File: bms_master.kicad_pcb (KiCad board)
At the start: 4 copper layers, 0 parts

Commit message: SCH[Sens & Inputs, Logic]: Started on sens and inputs condtiong, Logic page drawn. Need to add notes still.
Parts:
- added C1: 0.1 µF, remote_cl05a105ko5nnnc:C_0402_1005Metric, F.Cu at (155.5, 102.0)
- added C10: 0.1 µF, remote_cl05a105ko5nnnc:C_0402_1005Metric, F.Cu at (174.5, 97.9)
- added C11: 100 pF, remote_cl05a105ko5nnnc:C_0402_1005Metric, F.Cu at (150.6, 95.9)
- added C12: 100 pF, remote_cl05a105ko5nnnc:C_0402_1005Metric, F.Cu at (150.6, 97.9)
- added C13: 100 pF, remote_cl05a105ko5nnnc:C_0402_1005Metric, F.Cu at (150.6, 99.8)
- added C14: 100 pF, remote_cl05a105ko5nnnc:C_0402_1005Metric, F.Cu at (150.6, 101.8)
- added C15: 0.1 µF, remote_cl05a105ko5nnnc:C_0402_1005Metric, F.Cu at (155.5, 107.9)
- added C2: 4.7 nF, remote_cga3e3x7r1h474k080ae:C_0603_1608Metric, F.Cu at (160.3, 92.2)
- added C3: 0.1 µF, remote_cl05a105ko5nnnc:C_0402_1005Metric, F.Cu at (155.5, 104.0)
- added C4: 0.1 µF, remote_cl05a105ko5nnnc:C_0402_1005Metric, F.Cu at (155.5, 105.9)
- added C5: 100pF, remote_cl05a105ko5nnnc:C_0402_1005Metric, F.Cu at (150.6, 92.0)
- added C6: 100pF, remote_cl05a105ko5nnnc:C_0402_1005Metric, F.Cu at (150.6, 93.9)
- added C7: 220 nF, remote_cl05a105ko5nnnc:C_0402_1005Metric, F.Cu at (174.5, 92.0)
- added C8: 0.1 µF, remote_cl05a105ko5nnnc:C_0402_1005Metric, F.Cu at (174.5, 93.9)
- added C9: 220 nF, remote_cl05a105ko5nnnc:C_0402_1005Metric, F.Cu at (174.5, 95.9)
- added D1: PESD5V0U2BT-QR, remote_pesd5v0u2bt-qr:SOT-23-3, F.Cu at (148.8, 105.1)
- added D2: PESD5V0U2BT-QR, remote_pesd5v0u2bt-qr:SOT-23-3, F.Cu at (148.8, 109.6)
- added D3: Green, remote_ltst-c190tbkt:LED_0603_1608Metric, F.Cu at (156.3, 92.2)
- added D4: Green, remote_ltst-c190tbkt:LED_0603_1608Metric, F.Cu at (156.3, 94.7)
- added D5: RED, remote_ltst-c190tbkt:LED_0603_1608Metric, F.Cu at (156.3, 97.3)
- added D6: RED, remote_ltst-c190tbkt:LED_0603_1608Metric, F.Cu at (156.3, 99.8)
- added J1: 0436500200, remote_0436500200:CONN_SD-43650-001_02_MOL, F.Cu at (142.2, 79.2)
- added J2: 0430450200, remote_0430450200:CONN_SD-43045-001_02_MOL, F.Cu at (166.7, 65.1)
- added J3: TFM-115-02-S-D-WT, remote_tfm-115-02-s-d-wt:SAMTEC_TFM-115-02-S-D-WT, F.Cu at (148.6, 64.5)
- added J4: TFM-115-02-S-D-WT, remote_tfm-115-02-s-d-wt:SAMTEC_TFM-115-02-S-D-WT, F.Cu at (148.6, 72.9)
- added J7: 0436500600, remote_0436500600:CONN_SD-43650-001_06_MOL, F.Cu at (166.8, 79.2)
- added R1: 1k, remote_erj-2ge0r00x:R_0402_1005Metric, F.Cu at (147.7, 92.0)
- added R10: 1k, remote_erj-2ge0r00x:R_0402_1005Metric, F.Cu at (163.8, 92.0)
- added R11: 1k, remote_erj-2ge0r00x:R_0402_1005Metric, F.Cu at (163.8, 94.0)
- added R12: 10k, remote_erj-2ge0r00x:R_0402_1005Metric, F.Cu at (163.8, 96.0)
- added R13: 100k, remote_rcs060359r0fkea:R_0603_1608Metric, F.Cu at (160.3, 94.7)
- added R14: 10k, remote_erj-2ge0r00x:R_0402_1005Metric, F.Cu at (166.7, 92.0)
- added R15: 10k, remote_erj-2ge0r00x:R_0402_1005Metric, F.Cu at (166.7, 94.0)
- added R16: 10k, remote_erj-2ge0r00x:R_0402_1005Metric, F.Cu at (166.7, 96.0)
- added R17: 10k, remote_erj-2ge0r00x:R_0402_1005Metric, F.Cu at (169.6, 92.0)
- added R18: 1k, remote_erj-2ge0r00x:R_0402_1005Metric, F.Cu at (169.6, 94.0)
- added R19: 100k, remote_rcs060359r0fkea:R_0603_1608Metric, F.Cu at (160.3, 97.3)
- added R2: 1k, remote_erj-2ge0r00x:R_0402_1005Metric, F.Cu at (147.7, 94.0)
- added R20: 1k, remote_erj-2ge0r00x:R_0402_1005Metric, F.Cu at (169.6, 96.0)
- added R3: 49.9, remote_erj-2ge0r00x:R_0402_1005Metric, F.Cu at (147.7, 96.0)
- added R4: 49.9, remote_erj-2ge0r00x:R_0402_1005Metric, F.Cu at (147.7, 97.9)
- added R5: 49.9, remote_erj-2ge0r00x:R_0402_1005Metric, F.Cu at (147.7, 99.9)
- added R6: 49.9, remote_erj-2ge0r00x:R_0402_1005Metric, F.Cu at (147.7, 101.9)
- added R8: 10, remote_rcs060359r0fkea:R_0603_1608Metric, F.Cu at (178.0, 99.0)
- added R9: 100k, remote_rcs060359r0fkea:R_0603_1608Metric, F.Cu at (178.0, 101.5)
- added TH1: NCP18XH103F03RB, remote_rcs060359r0fkea:R_0603_1608Metric, F.Cu at (175.1, 110.3)
- added U1: BQ79600PWRQ1, remote_bq79600pwrq1:SOIC_9600PWQ1_TEX, F.Cu at (180.4, 94.4)
- added U2: SM91502ALA-E, remote_sm91502ala-e:IC6_SM91502ALA-E_BRN, F.Cu at (140.6, 96.5)
- added U3: SM91502ALA-E, remote_sm91502ala-e:IC6_SM91502ALA-E_BRN, F.Cu at (140.6, 107.6)
- added U4: SN74LVC1G11IDCKRQ1, remote_sn74lvc1g11idckrq1:DCK6, F.Cu at (166.3, 100.7)
- added U5: SN74LVC1G07DCKT, remote_sn74lvc1g07dckt:DCK5, F.Cu at (165.9, 104.7)
- added U6: TPS3430WDRCR, remote_tps3430wdrcr:DRC0010J_NV, F.Cu at (161.2, 100.8)
- added U7: SN74LVC2G04DCKR, remote_sn74lvc2g04dckr:DCK0006A_N, F.Cu at (160.9, 104.9)
- added U8: TLP293(GB-TPL,E, remote_tlp293_gb-tpl_e:SO4_TOS, F.Cu at (178.0, 106.9)

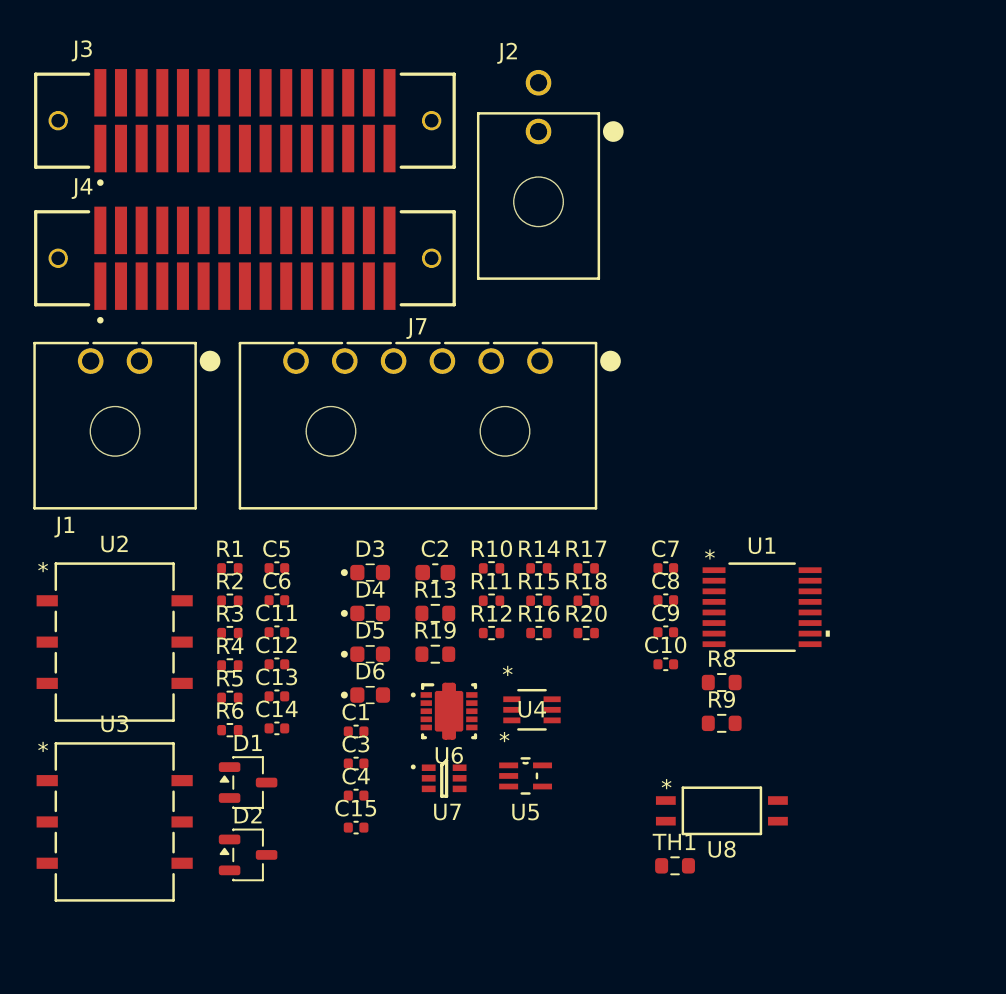
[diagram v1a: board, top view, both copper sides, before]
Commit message: SCH[Logic, Connectors]: Removed watchdog timer going to use just stm32 interal watchdog, and com master faults. This is to simplfiy hardware less parts not needed. Adding DNP conector for halleffect sensor.
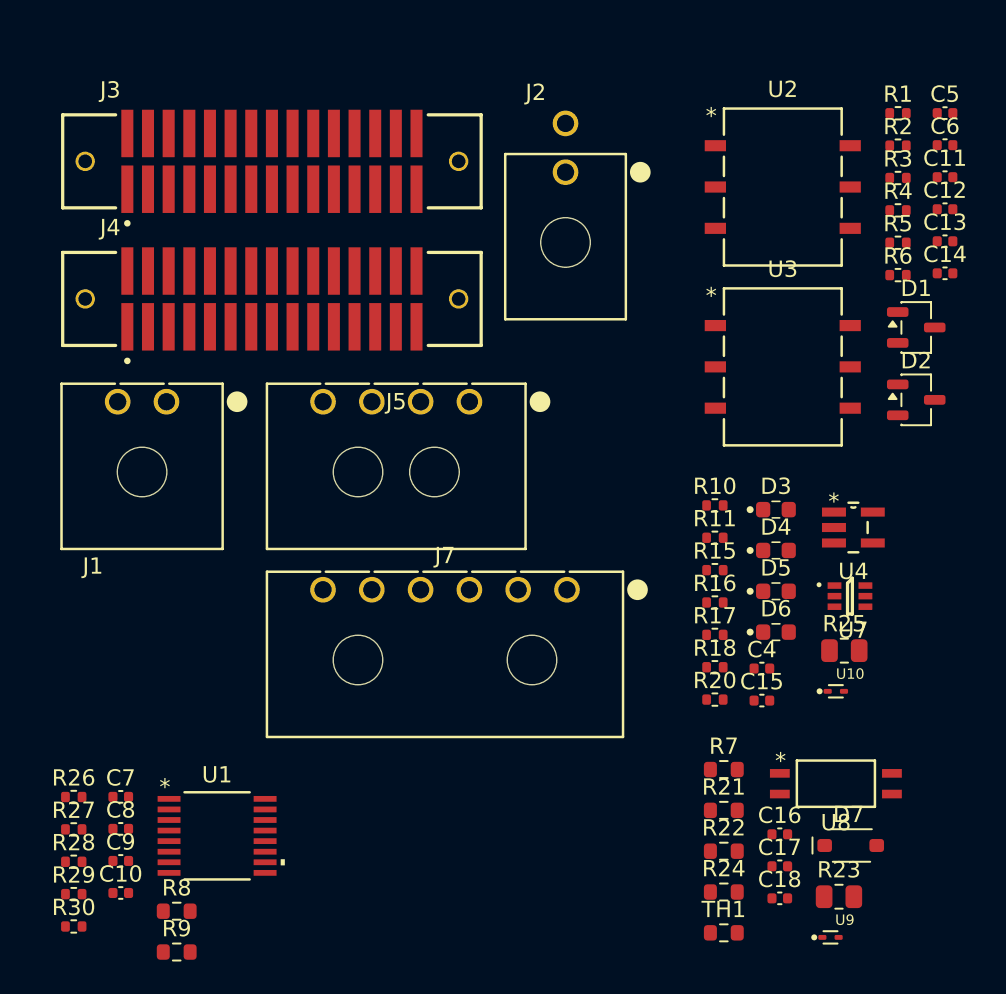
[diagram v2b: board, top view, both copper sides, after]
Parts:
- removed C1, C3: 0.1 µF, remote_cl05a105ko5nnnc:C_0402_1005Metric
- removed C2: 4.7 nF, remote_cga3e3x7r1h474k080ae:C_0603_1608Metric
- removed R12, R14: 10k, remote_erj-2ge0r00x:R_0402_1005Metric
- removed R13, R19: 100k, remote_rcs060359r0fkea:R_0603_1608Metric
- removed U5: SN74LVC1G07DCKT, remote_sn74lvc1g07dckt:DCK5
- removed U6: TPS3430WDRCR, remote_tps3430wdrcr:DRC0010J_NV
- added C16: 0.1 µF, remote_cl05a105ko5nnnc:C_0402_1005Metric, F.Cu at (181.5, 108.3)
- added C17: 10 nF, remote_cl05a105ko5nnnc:C_0402_1005Metric, F.Cu at (181.5, 110.3)
- added C18: 10 nF, remote_cl05a105ko5nnnc:C_0402_1005Metric, F.Cu at (181.5, 112.3)
- added D7: 1N4148W, remote_1n4148w:P35_SOD-123F, F.Cu at (184.3, 109.0)
- added J5: 0436500400, remote_0436500400:CONN_SD-43650-001_04_MOL, F.Cu at (162.4, 81.7)
- added R21: 10k, remote_rcs060359r0fkea:R_0603_1608Metric, F.Cu at (178.1, 106.9)
- added R22: 10k, remote_rcs060359r0fkea:R_0603_1608Metric, F.Cu at (178.1, 109.4)
- added R23: 10k, remote_crcw080510k0fkea:R_0805_2012Metric, F.Cu at (185.2, 112.2)
- added R24: 22k, remote_rcs060359r0fkea:R_0603_1608Metric, F.Cu at (178.1, 111.9)
- added R25: 330, remote_crcw080510k0fkea:R_0805_2012Metric, F.Cu at (185.5, 97.0)
- added R26: 10k, remote_erj-2ge0r00x:R_0402_1005Metric, F.Cu at (138.1, 106.0)
- added R27: 10k, remote_erj-2ge0r00x:R_0402_1005Metric, F.Cu at (138.1, 108.0)
- added R28: 10k, remote_erj-2ge0r00x:R_0402_1005Metric, F.Cu at (138.1, 110.0)
- added R29: 10k, remote_erj-2ge0r00x:R_0402_1005Metric, F.Cu at (138.1, 112.0)
- added R30: 10k, remote_erj-2ge0r00x:R_0402_1005Metric, F.Cu at (138.1, 114.0)
- added R7: 10k, remote_rcs060359r0fkea:R_0603_1608Metric, F.Cu at (178.1, 104.3)
- added U10: ESD9B5.0ST5G, remote_esd9b3.3st5g:SODFL1006X40N, F.Cu at (185.0, 99.5)
- added U9: ESD9B5.0ST5G, remote_esd9b3.3st5g:SODFL1006X40N, F.Cu at (184.6, 114.7)
- U4: value SN74LVC1G11IDCKRQ1 -> SN74LVC1G08QDBVRQ1; footprint remote_sn74lvc1g11idckrq1:DCK6 -> remote_sn74lvc1g08qdbvrq1:DBV5
- moved C11 49.7 mm to (191.7, 67.9)
- moved C12 49.7 mm to (191.7, 69.9)
- moved C13 49.7 mm to (191.7, 71.9)
- moved C14 49.7 mm to (191.7, 73.8)
- moved C5 49.7 mm to (191.7, 64.0)
- moved C6 49.7 mm to (191.7, 66.0)
- moved U2 49.7 mm to (181.7, 68.5)
- moved U3 49.7 mm to (181.7, 79.6)
- moved D2 49.7 mm to (189.9, 81.6)
- moved R1 49.7 mm to (188.8, 64.0)
- moved R2 49.7 mm to (188.8, 66.0)
- moved R3 49.7 mm to (188.8, 68.0)
- moved R5 49.7 mm to (188.8, 72.0)
- moved R6 49.7 mm to (188.8, 73.9)
- moved D1 49.7 mm to (189.9, 77.2)
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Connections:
- J3 pad 12: /Project Architecture/Connectors/SDC_OK_N -> unconnected-(J3-TIM2_CH1-Pad12)
- J3 pad 13: /Project Architecture/Connectors/CHG_MODE_N -> unconnected-(J3-TIM2_CH3-Pad13)
- J3 pad 16: /Project Architecture/BMS_OK & watchdog/FB.NFAULT -> /Project Architecture/Connectors/FB.NFAULT
- J3 pad 18: /Project Architecture/BMS_OK & watchdog/WDT_KICK -> /Project Architecture/Connectors/CHG_MODE_N
- J3 pad 19: /Project Architecture/BMS_OK & watchdog/FB.BMS_OK -> /Project Architecture/Connectors/FB.BMS_OK
- J3 pad 20: /Project Architecture/BMS_OK & watchdog/FB.WDT_OK -> /Project Architecture/Connectors/SDC_OK_N
- R11 pad 2: /Project Architecture/BMS_OK & watchdog/BMS_OK -> /Project Architecture/BMS_OK & watchdog/BMS_OK_LOGIC
- R16 pad 1: /Project Architecture/BMS_OK & watchdog/BMS_OK -> /Project Architecture/BMS_OK & watchdog/BMS_OK_LOGIC
- TH1 pad 1: unconnected-(TH1-Pad1) -> /Project Architecture/Inputs & Sensing/+3V3
- TH1 pad 2: unconnected-(TH1-Pad2) -> /Project Architecture/Connectors/BOARD_TEMP
- U4 pad 1: /Project Architecture/BMS_OK & watchdog/WDT_OK -> /Project Architecture/Connectors/MCU_BMS_OK
- U4 pad 2: /Project Architecture/GND -> /Project Architecture/BMS_OK & watchdog/NFAULT
- U4 pad 3: /Project Architecture/Connectors/MCU_BMS_OK -> /Project Architecture/GND
- U4 pad 4: /Project Architecture/BMS_OK & watchdog/BMS_OK -> /Project Architecture/BMS_OK & watchdog/BMS_OK_LOGIC
- U7 pad 1: /Project Architecture/BMS_OK & watchdog/FB.WDT_OK -> /Project Architecture/BMS_OK & watchdog/FB.BMS_OK
- U8 pad 1: unconnected-(U8-Pad1) -> Net-(D7-K)
- U8 pad 2: unconnected-(U8-Pad2) -> /Project Architecture/Connectors/SDC_SENSE_RTN
- U8 pad 3: unconnected-(U8-Pad3) -> /Project Architecture/Inputs & Sensing/GND
- U8 pad 4: unconnected-(U8-Pad4) -> /Project Architecture/Connectors/SDC_OK_N

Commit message: PCB[Daisy]: Inital layout for this.
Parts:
- removed C11, C12, C13, C14: 100 pF, remote_cl05a105ko5nnnc:C_0402_1005Metric
- removed C15, C16, C4: 0.1 µF, remote_cl05a105ko5nnnc:C_0402_1005Metric
- removed C17, C18: 10 nF, remote_cl05a105ko5nnnc:C_0402_1005Metric
- removed D3, D4: Green, remote_ltst-c190tbkt:LED_0603_1608Metric
- removed D5, D6: RED, remote_ltst-c190tbkt:LED_0603_1608Metric
- removed D7: 1N4148W, remote_1n4148w:P35_SOD-123F
- removed J2: 0430450200, remote_0430450200:CONN_SD-43045-001_02_MOL
- removed J5: 0436500400, remote_0436500400:CONN_SD-43650-001_04_MOL
- removed J7: 0436500600, remote_0436500600:CONN_SD-43650-001_06_MOL
- removed R1, R18, R2, R20: 1k, remote_erj-2ge0r00x:R_0402_1005Metric
- removed R15, R16, R17, R26, R27, R28, R29, R30: 10k, remote_erj-2ge0r00x:R_0402_1005Metric
- removed R21, R22, R7: 10k, remote_rcs060359r0fkea:R_0603_1608Metric
- removed R23: 10k, remote_crcw080510k0fkea:R_0805_2012Metric
- removed R24: 22k, remote_rcs060359r0fkea:R_0603_1608Metric
- removed R25: 330, remote_crcw080510k0fkea:R_0805_2012Metric
- removed R3, R4, R5, R6: 49.9, remote_erj-2ge0r00x:R_0402_1005Metric
- removed TH1: NCP18XH103F03RB, remote_rcs060359r0fkea:R_0603_1608Metric
- removed U1: BQ79600PWRQ1, remote_bq79600pwrq1:SOIC_9600PWQ1_TEX
- removed U10, U9: ESD9B5.0ST5G, remote_esd9b3.3st5g:SODFL1006X40N
- removed U4: SN74LVC1G08QDBVRQ1, remote_sn74lvc1g08qdbvrq1:DBV5
- removed U7: SN74LVC2G04DCKR, remote_sn74lvc2g04dckr:DCK0006A_N
- removed U8: TLP293(GB-TPL,E, remote_tlp293_gb-tpl_e:SO4_TOS
- added H1: MountingHole, MountingHole:MountingHole_3.2mm_M3, F.Cu at (3.48, 3.48)
- added H2: MountingHole, MountingHole:MountingHole_3.2mm_M3, F.Cu at (3.48, 11.4)
- added H3: MountingHole, MountingHole:MountingHole_3.2mm_M3, F.Cu at (3.48, 19.4)
- added H4: MountingHole, MountingHole:MountingHole_3.2mm_M3, F.Cu at (3.48, 27.3)
- added H5: MountingHole, MountingHole:MountingHole_3.2mm_M3, F.Cu at (3.48, 35.3)
- added J4: 0436500200, remote_0436500200:CONN_SD-43650-001_02_MOL, F.Cu at (221.2, 94.0)
- added R12: 1k, remote_erj-2ge0r00x:R_0402_1005Metric, F.Cu at (197.8, 95.5)
- added R13: 49.9, remote_erj-2ge0r00x:R_0402_1005Metric, F.Cu at (200.2, 96.5)
- C10, C8: value 0.1 µF -> 100 pF
- C5: value 100pF -> 100 pF
- C7: value 220 nF -> 100 pF
- C9: value 220 nF -> 100pF
- D1, D2: footprint remote_pesd5v0u2bt-qr:SOT-23-3 -> remote_pesd1can_215:SOT23_PESD1_NEX
- J1: value 0436500200 -> 0430450200; footprint remote_0436500200:CONN_SD-43650-001_02_MOL -> remote_0430450200:CONN_SD-43045-001_02_MOL
- R10, R11: value 1k -> 49.9
- R8: value 10 -> 49.9; footprint remote_rcs060359r0fkea:R_0603_1608Metric -> remote_erj-2ge0r00x:R_0402_1005Metric
- R9: value 100k -> 1k; footprint remote_rcs060359r0fkea:R_0603_1608Metric -> remote_erj-2ge0r00x:R_0402_1005Metric
- moved J1 77.6 mm to (221.2, 76.5), turned to 90 degrees
- moved R8 67.2 mm to (200.2, 75.5)
- moved C9 66.5 mm to (206.0, 95.5), turned to 180 degrees
- moved R9 66.1 mm to (197.8, 76.4), turned to -90 degrees
- moved C7 64.2 mm to (198.8, 77.9), turned to -90 degrees
- moved C10 59.7 mm to (198.8, 96.9), turned to -90 degrees
- moved C8 59.4 mm to (198.8, 94.1), turned to 90 degrees
- moved J4 47.9 mm to (107.5, 97.0)
- moved J3 42.8 mm to (107.5, 65.0)
- moved U3 34.2 mm to (212.0, 95.5)
- moved U2 31.3 mm to (212.0, 76.5)
- moved R10 25.0 mm to (200.2, 77.5)
- moved R11 23.1 mm to (200.2, 94.5)
- moved D2 19.1 mm to (203.1, 95.5)
- moved C6 17.8 mm to (206.0, 76.5), turned to 180 degrees
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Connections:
- C10 pad 1: /Project Architecture/Com. Chip/BAT -> /Project Architecture/GND
- C10 pad 2: /Project Architecture/GND -> /Project Architecture/Com. Chip/U1_COML.P
- C5 pad 1: /Project Architecture/Daisy Chain/COMH_CT -> /Project Architecture/GND
- C5 pad 2: /Project Architecture/GND -> /Project Architecture/Com. Chip/U1_COMH.P
- C6 pad 1: /Project Architecture/Daisy Chain/COML_CT -> /Project Architecture/Daisy Chain/COMH_CT
- C7 pad 2: /Project Architecture/Com. Chip/DVDD -> /Project Architecture/Com. Chip/U1_COMH.N
- C8 pad 1: /Project Architecture/+3V3 -> /Project Architecture/GND
- C8 pad 2: /Project Architecture/GND -> /Project Architecture/Com. Chip/U1_COML.N
- C9 pad 1: /Project Architecture/Com. Chip/CVDD -> /Project Architecture/Daisy Chain/COML_CT
- J1 pad 1: /Project Architecture/Connectors/COML.N -> /Project Architecture/Connectors/COMH.N
- J1 pad 2: /Project Architecture/Connectors/COML.P -> /Project Architecture/Connectors/COMH.P
- J3 pad 01: /Project Architecture/+12V -> /Project Architecture/Connectors/BOARD_TEMP
- J3 pad 02: /Project Architecture/+12V -> /Project Architecture/Connectors/BOARD_TEMP
- J3 pad 03: /Project Architecture/+5V -> /Project Architecture/GND
- J3 pad 04: /Project Architecture/+5V -> /Project Architecture/GND
- J3 pad 05: /Project Architecture/+3V3 -> unconnected-(J3-ADC1_IN2-Pad05)
- J3 pad 06: /Project Architecture/+3V3 -> unconnected-(J3-ADC1_IN2-Pad06)
- J3 pad 11: unconnected-(J3-TIM1_CH3-Pad11) -> /Project Architecture/GND
- J3 pad 12: unconnected-(J3-TIM2_CH1-Pad12) -> /Project Architecture/GND
- J3 pad 14: /Project Architecture/Com. Chip/SPI.nCS -> unconnected-(J3-ADC1_IN4-Pad14)
- J3 pad 15: /Project Architecture/Com. Chip/SPI.RDY -> /Project Architecture/GND
- J3 pad 16: /Project Architecture/Connectors/FB.NFAULT -> /Project Architecture/GND
- J3 pad 17: /Project Architecture/Connectors/MCU_BMS_OK -> unconnected-(J3-ADC2_IN5-Pad17)
- J3 pad 18: /Project Architecture/Connectors/CHG_MODE_N -> unconnected-(J3-ADC2_IN5-Pad18)
- J3 pad 19: /Project Architecture/Connectors/FB.BMS_OK -> /Project Architecture/GND
- J3 pad 20: /Project Architecture/Connectors/SDC_OK_N -> /Project Architecture/GND
- J3 pad 21: /Project Architecture/Com. Chip/SPI.MOSI -> unconnected-(J3-DAC1_OUT2-Pad21)
- J3 pad 22: /Project Architecture/Com. Chip/SPI.MISO -> unconnected-(J3-DAC1_OUT2-Pad22)
- J3 pad 25: /Project Architecture/GND -> unconnected-(J3-DAC1_OUT1-Pad25)
- J3 pad 26: /Project Architecture/Com. Chip/SPI.SCLK -> unconnected-(J3-DAC1_OUT1-Pad26)
- J3 pad 29: unconnected-(J3-I2C1_SCL-Pad29) -> /Project Architecture/GND
- J3 pad 30: unconnected-(J3-I2C1_SDA-Pad30) -> /Project Architecture/GND
- R10 pad 1: Net-(D3-A) -> /Project Architecture/Com. Chip/U1_COMH.N
- R10 pad 2: /Project Architecture/+3V3 -> /Project Architecture/Daisy Chain/COMH_WN
- R11 pad 1: Net-(D4-A) -> /Project Architecture/Com. Chip/U1_COML.N
- R11 pad 2: /Project Architecture/BMS_OK & watchdog/BMS_OK_LOGIC -> /Project Architecture/Daisy Chain/COML_WN
- R8 pad 1: /Project Architecture/Com. Chip/BAT -> /Project Architecture/Com. Chip/U1_COMH.P
- R8 pad 2: /Project Architecture/+12V -> /Project Architecture/Daisy Chain/COMH_WP
- R9 pad 1: /Project Architecture/BMS_OK & watchdog/NFAULT -> /Project Architecture/Com. Chip/U1_COMH.P
- R9 pad 2: /Project Architecture/+3V3 -> /Project Architecture/Com. Chip/U1_COMH.N
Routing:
- net (no net): track 0.00 -> 8.39 mm
- net /Project Architecture/Daisy Chain/COML_WP: track 0.00 -> 7.85 mm
- net /Project Architecture/Daisy Chain/COML_WN: track 0.00 -> 7.85 mm
- net /Project Architecture/Daisy Chain/COMH_WP: track 0.00 -> 7.80 mm
- net /Project Architecture/Daisy Chain/COMH_WN: track 0.00 -> 7.80 mm
- net /Project Architecture/Connectors/COML.P: track 0.00 -> 6.59 mm
- net /Project Architecture/Connectors/COML.N: track 0.00 -> 6.59 mm
- net /Project Architecture/Connectors/COMH.N: track 0.00 -> 6.38 mm
- net /Project Architecture/Connectors/COMH.P: track 0.00 -> 6.35 mm
- net /Project Architecture/GND: track 0.00 -> 4.49 mm, vias 0 -> 2
- net /Project Architecture/Daisy Chain/COML_CT: track 0.00 -> 1.42 mm
- net /Project Architecture/Daisy Chain/COMH_CT: track 0.00 -> 1.37 mm
- net /Project Architecture/Com. Chip/U1_COML.P: track 0.00 -> 0.84 mm, vias 0 -> 1
- net /Project Architecture/Com. Chip/U1_COML.N: track 0.00 -> 0.84 mm, vias 0 -> 1
- net /Project Architecture/Com. Chip/U1_COMH.P: track 0.00 -> 0.84 mm, vias 0 -> 1
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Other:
- board outline added: 100 x 50 mm
- board text added: "COMHN"
- board text added: "COMHP"
- board text added: "COMLN"
- board text added: "COMLP"
- board text added: "ISOLATION ZONE"
